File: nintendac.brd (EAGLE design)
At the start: 43 x 43 mm, 35 parts, among them IC2 REG1117, U1 STM32F10XRXT6, X1 USB-MICROB

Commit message: vcc trace update
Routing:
- net +3V3: track 21.1 -> 25.8 mm
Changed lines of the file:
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@@
 <wire x1="13.2376" y1="29.928" x2="12.7364" y2="30.4292" width="0.254" layer="1"/>
 <contactref element="R8" pad="2"/>
-<wire x1="15.128" y1="23.428" x2="17.0018" y2="23.428" width="0.3048" layer="1"/>
-<wire x1="17.0018" y1="23.428" x2="18.2626" y2="24.6888" width="0.3048" layer="1"/>
 <wire x1="14.02219375" y1="22.48039375" x2="14.18039375" y2="22.48039375" width="0.2032" layer="1"/>
 <wire x1="14.18039375" y1="22.48039375" x2="15.128" y2="23.428" width="0.2032" layer="1"/>
@@
 <wire x1="15.1348" y1="29.9212" x2="15.128" y2="29.928" width="0.2032" layer="1"/>
 <contactref element="JP1" pad="1"/>
+<wire x1="15.128" y1="23.428" x2="16.824" y2="23.428" width="0.2032" layer="1"/>
+<wire x1="16.824" y1="23.428" x2="17.653" y2="24.257" width="0.2032" layer="1"/>
+<wire x1="17.653" y1="24.257" x2="17.653" y2="29.21" width="0.2032" layer="1"/>
+<wire x1="17.653" y1="29.21" x2="17.272" y2="29.591" width="0.2032" layer="1"/>
 </signal>
 <signal name="N$1">

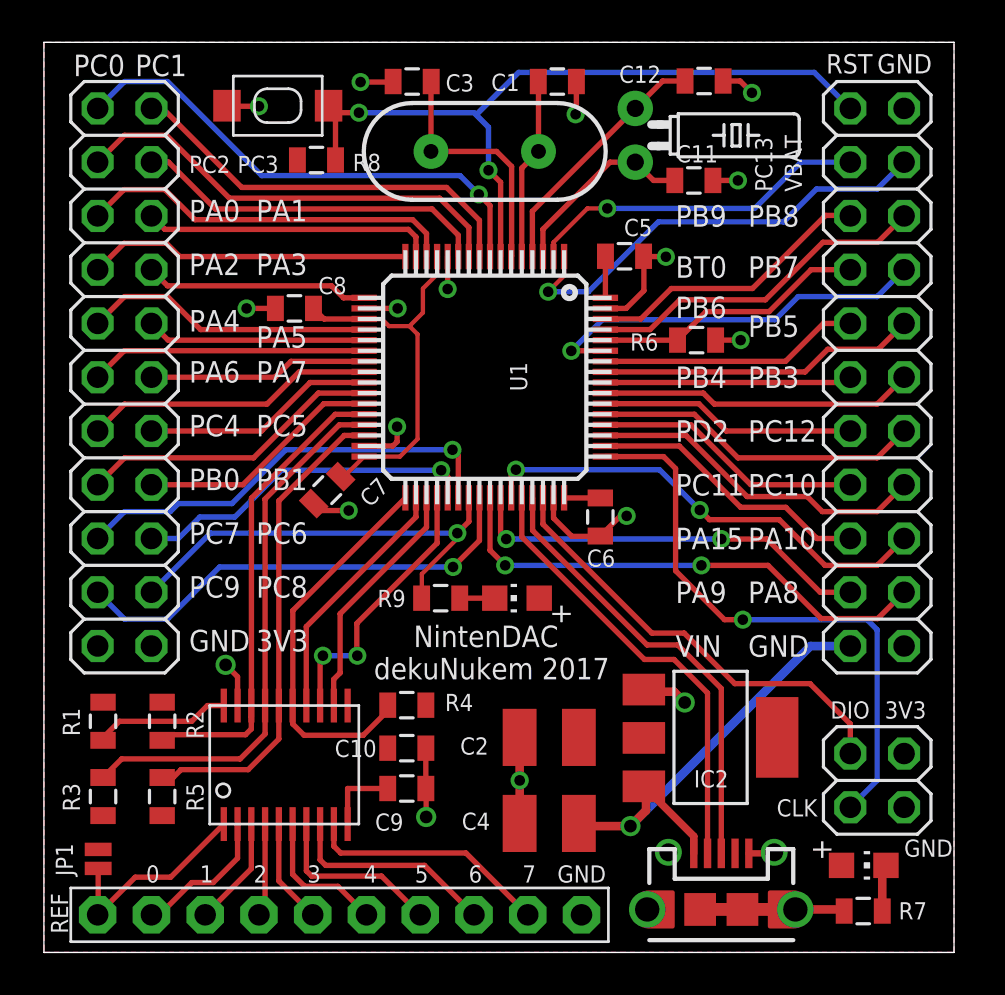
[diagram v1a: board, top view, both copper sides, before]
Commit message: added a resistor on ref
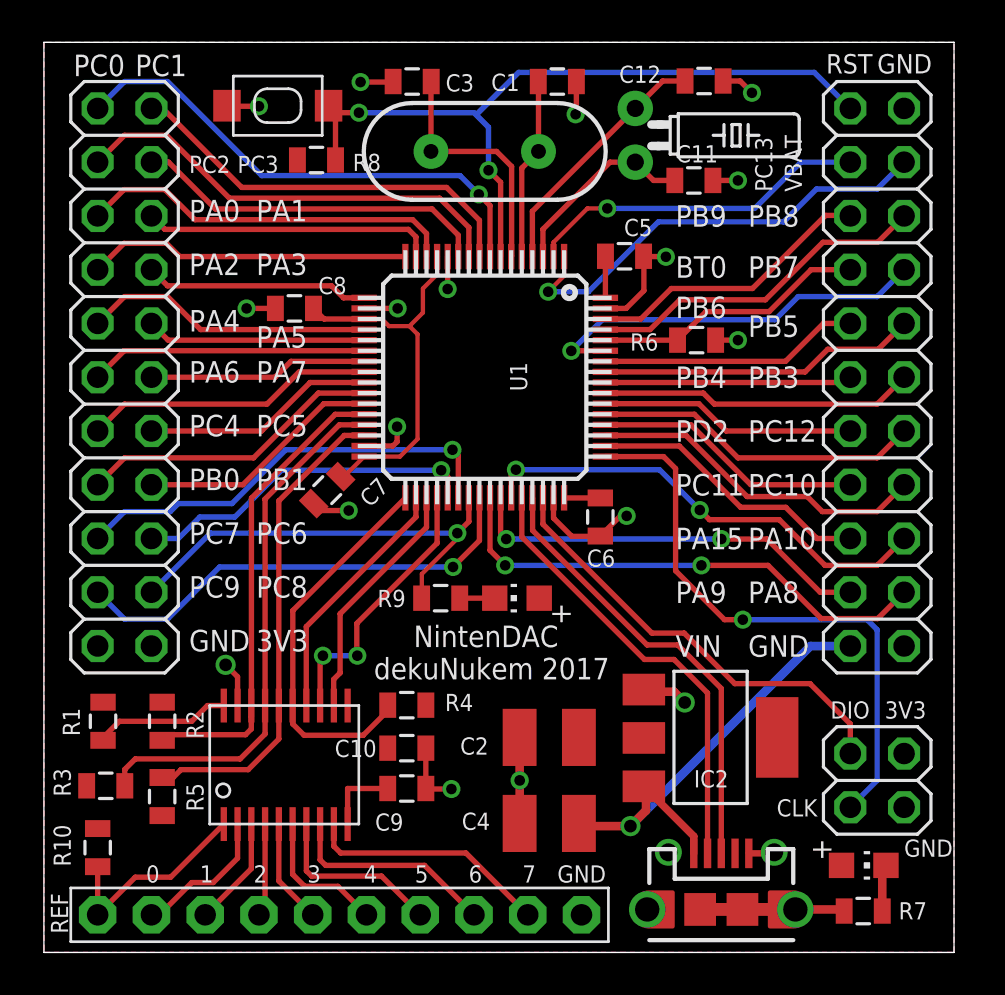
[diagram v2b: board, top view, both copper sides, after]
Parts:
- removed JP1: JUMPER-PAD-2-NO, SparkFun-Passives:PAD-JUMPER-2-NO_NO_SILK
- added R10: (no value), SparkFun-Passives:0805
- moved R3 0.52 mm to (2.92, 7.87), turned to 180 degrees
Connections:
- net +3V3: now also R10.2; no longer JP1.1
- net N$7: now also R10.1; no longer JP1.2
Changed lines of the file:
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@@
 <attribute name="VALUE" x="7.874" y="10.16" size="1.27" layer="27" rot="R90"/>
 </element>
-<element name="R3" library="SparkFun-Passives" package="0805" value="" x="2.794" y="7.366" smashed="yes" rot="R270">
-<attribute name="NAME" x="0.889" y="8.001" size="0.8128" layer="25" rot="R270"/>
-<attribute name="VALUE" x="0.508" y="8.128" size="1.27" layer="27" rot="R270"/>
+<element name="R3" library="SparkFun-Passives" package="0805" value="" x="2.921" y="7.874" smashed="yes" rot="R180">
+<attribute name="NAME" x="1.27" y="7.366" size="0.8128" layer="25" rot="R90"/>
+<attribute name="VALUE" x="3.683" y="10.16" size="1.27" layer="27" rot="R180"/>
 </element>
 <element name="R4" library="SparkFun-Passives" package="0805" value="" x="17.145" y="11.684" smashed="yes">
@@
 <attribute name="VALUE" x="19.7612" y="18.1356" size="0.4064" layer="27" rot="R180"/>
 </element>
-<element name="JP1" library="SparkFun-Passives" package="PAD-JUMPER-2-NO_NO_SILK" value="JUMPER-PAD-2-NO" x="2.5654" y="4.4196" smashed="yes" rot="R270">
-<attribute name="NAME" x="1.3716" y="3.6132" size="0.8128" layer="25" rot="R90"/>
+<element name="R10" library="SparkFun-Passives" package="0805" value="" x="2.54" y="4.953" smashed="yes" rot="R90">
+<attribute name="NAME" x="1.27" y="4.064" size="0.8128" layer="25" rot="R90"/>
+<attribute name="VALUE" x="3.937" y="3.937" size="0.4064" layer="27" rot="R90"/>
 </element>
 </elements>
@@
 <contactref element="R6" pad="1"/>
 <wire x1="18.045" y1="7.747" x2="18.045" y2="9.652" width="0.254" layer="1"/>
-<via x="18.0594" y="6.4008" extent="1-16" drill="0.6"/>
+<via x="19.2532" y="7.7216" extent="1-16" drill="0.5"/>
 <wire x1="35.504" y1="2.032" x2="33.004" y2="2.032" width="0.6096" layer="1"/>
 <wire x1="33.004" y1="2.032" x2="31.004" y2="2.032" width="0.6096" layer="1"/>
@@
 <wire x1="28.3464" y1="31.2674" x2="28.3464" y2="32.8786" width="0.254" layer="1"/>
 <wire x1="28.3464" y1="32.8786" x2="28.332" y2="32.893" width="0.254" layer="1"/>
-<via x="32.9184" y="28.9306" extent="1-16" drill="0.5"/>
-<wire x1="31.7356" y1="28.9306" x2="32.9184" y2="28.9306" width="0.254" layer="1"/>
+<via x="32.7914" y="28.9306" extent="1-16" drill="0.5"/>
+<wire x1="31.7356" y1="28.9306" x2="32.7914" y2="28.9306" width="0.254" layer="1"/>
 <contactref element="JP4" pad="4"/>
 <contactref element="JP2" pad="1"/>
@@
 <via x="29.3878" y="32.8676" extent="1-16" drill="0.5"/>
 <wire x1="12.647803125" y1="21.207603125" x2="12.749403125" y2="21.207603125" width="0.254" layer="1"/>
-<wire x1="18.0594" y1="6.4008" x2="18.0594" y2="7.7326" width="0.254" layer="1"/>
-<wire x1="18.0594" y1="7.7326" x2="18.045" y2="7.747" width="0.254" layer="1"/>
+<wire x1="18.0704" y1="7.7216" x2="18.045" y2="7.747" width="0.254" layer="1"/>
 <wire x1="12.749403125" y1="21.207603125" x2="12.828396875" y2="21.207603125" width="0.254" layer="1"/>
 <wire x1="14.4018" y1="20.8788" x2="13.07820625" y2="20.8788" width="0.254" layer="1"/>
@@
 <wire x1="28.2448" y1="12.319" x2="29.7688" y2="12.319" width="0.4064" layer="1"/>
 <wire x1="29.7688" y1="12.319" x2="30.2768" y2="11.811" width="0.4064" layer="1"/>
+<wire x1="18.0704" y1="7.7216" x2="19.2532" y2="7.7216" width="0.254" layer="1"/>
 <wire x1="28.2448" y1="12.319" x2="28.3464" y2="12.4206" width="0" layer="19" extent="1-1"/>
 </signal>
@@
 <wire x1="15.9766" y1="29.9212" x2="15.1348" y2="29.9212" width="0.2032" layer="1"/>
 <wire x1="15.1348" y1="29.9212" x2="15.128" y2="29.928" width="0.2032" layer="1"/>
-<contactref element="JP1" pad="1"/>
 <wire x1="15.128" y1="23.428" x2="16.824" y2="23.428" width="0.2032" layer="1"/>
 <wire x1="16.824" y1="23.428" x2="17.653" y2="24.257" width="0.2032" layer="1"/>
 <wire x1="17.653" y1="24.257" x2="17.653" y2="29.21" width="0.2032" layer="1"/>
 <wire x1="17.653" y1="29.21" x2="17.272" y2="29.591" width="0.2032" layer="1"/>
+<contactref element="R10" pad="2"/>
 </signal>
 <signal name="N$1">
@@
 <wire x1="5.991" y1="3.556" x2="4.318" y2="3.556" width="0.254" layer="1"/>
 <wire x1="4.318" y1="3.556" x2="2.54" y2="1.778" width="0.254" layer="1"/>
-<contactref element="JP1" pad="2"/>
-<wire x1="2.5654" y1="3.9696" x2="2.5654" y2="1.8034" width="0.254" layer="1"/>
 <wire x1="2.5654" y1="1.8034" x2="2.54" y2="1.778" width="0.254" layer="1"/>
+<contactref element="R10" pad="1"/>
+<wire x1="2.54" y1="4.053" x2="2.54" y2="1.778" width="0.254" layer="1"/>
 </signal>
 <signal name="N$8">
@@
 <wire x1="13.9552" y1="24.928" x2="10.4394" y2="21.4122" width="0.254" layer="1"/>
 <wire x1="10.4394" y1="11.6756" x2="10.45" y2="11.665" width="0.254" layer="1"/>
-<wire x1="9.271" y1="9.144" x2="3.672" y2="9.144" width="0.254" layer="1"/>
-<wire x1="3.672" y1="9.144" x2="2.794" y2="8.266" width="0.254" layer="1"/>
 <wire x1="10.45" y1="10.323" x2="9.271" y2="9.144" width="0.254" layer="1"/>
 <wire x1="10.45" y1="10.323" x2="10.45" y2="11.665" width="0.254" layer="1"/>
 <wire x1="10.45" y1="11.665" x2="10.45" y2="21.4016" width="0.254" layer="1"/>
 <wire x1="10.45" y1="21.4016" x2="10.4394" y2="21.4122" width="0.254" layer="1"/>
+<wire x1="9.271" y1="9.144" x2="4.318" y2="9.144" width="0.254" layer="1"/>
+<wire x1="4.318" y1="9.144" x2="3.821" y2="8.647" width="0.254" layer="1"/>
+<wire x1="3.821" y1="8.647" x2="3.821" y2="7.874" width="0.254" layer="1"/>
 </signal>
 <signal name="N$3">
